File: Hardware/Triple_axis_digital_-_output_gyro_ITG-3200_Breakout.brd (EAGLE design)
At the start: 17.8 x 21.6 mm, 17 parts, among them U1 ITG-32001:1

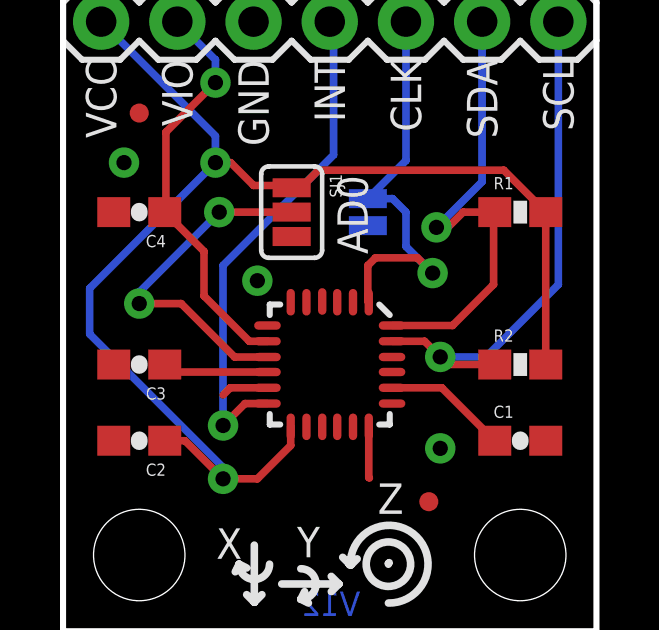
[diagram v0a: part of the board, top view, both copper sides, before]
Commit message: Changed a few trace routes
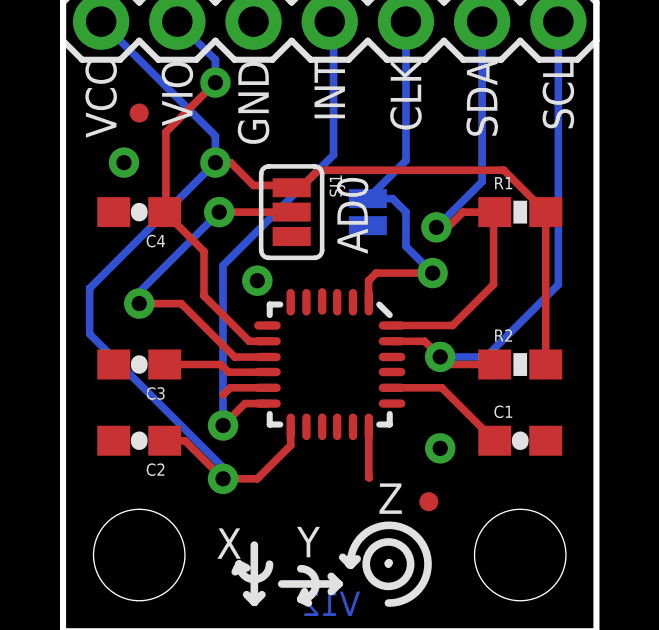
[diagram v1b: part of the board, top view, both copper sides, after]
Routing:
- net CLKIN: track 14.0 -> 13.2 mm
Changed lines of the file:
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@@
 <wire x1="33.02" y1="-3.683" x2="33.909" y2="-4.572" width="0.254" layer="16"/>
 <via x="33.909" y="-4.572" extent="1-16" drill="0.508"/>
-<wire x1="33.909" y1="-4.572" x2="33.401" y2="-4.064" width="0.254" layer="1"/>
-<wire x1="33.401" y1="-4.064" x2="32.004" y2="-4.064" width="0.254" layer="1"/>
-<wire x1="32.004" y1="-4.064" x2="31.75" y2="-4.318" width="0.254" layer="1"/>
-<wire x1="31.75" y1="-4.318" x2="31.75" y2="-5.513" width="0.254" layer="1"/>
-<wire x1="31.75" y1="-5.513" x2="31.7808" y2="-5.5438" width="0.254" layer="1"/>
+<wire x1="31.7808" y1="-5.5438" x2="31.7754" y2="-5.5384" width="0.254" layer="1"/>
+<wire x1="31.7754" y1="-5.5384" x2="31.7754" y2="-4.826" width="0.254" layer="1"/>
+<wire x1="31.7754" y1="-4.826" x2="32.0294" y2="-4.572" width="0.254" layer="1"/>
+<wire x1="32.0294" y1="-4.572" x2="33.909" y2="-4.572" width="0.254" layer="1"/>
 </signal>
 <signal name="INT">
@@
 <contactref element="C3" pad="1"/>
 <contactref element="U1" pad="10"/>
-<wire x1="28.4038" y1="-7.87" x2="25.23" y2="-7.87" width="0.254" layer="1"/>
-<wire x1="25.23" y1="-7.87" x2="24.98" y2="-7.62" width="0.254" layer="1"/>
+<wire x1="28.4038" y1="-7.87" x2="28.3998" y2="-7.874" width="0.254" layer="1"/>
+<wire x1="28.3998" y1="-7.874" x2="27.1018" y2="-7.874" width="0.254" layer="1"/>
+<wire x1="27.1018" y1="-7.874" x2="26.8478" y2="-7.62" width="0.254" layer="1"/>
+<wire x1="26.8478" y1="-7.62" x2="24.98" y2="-7.62" width="0.254" layer="1"/>
 </signal>
 <signal name="N$1">

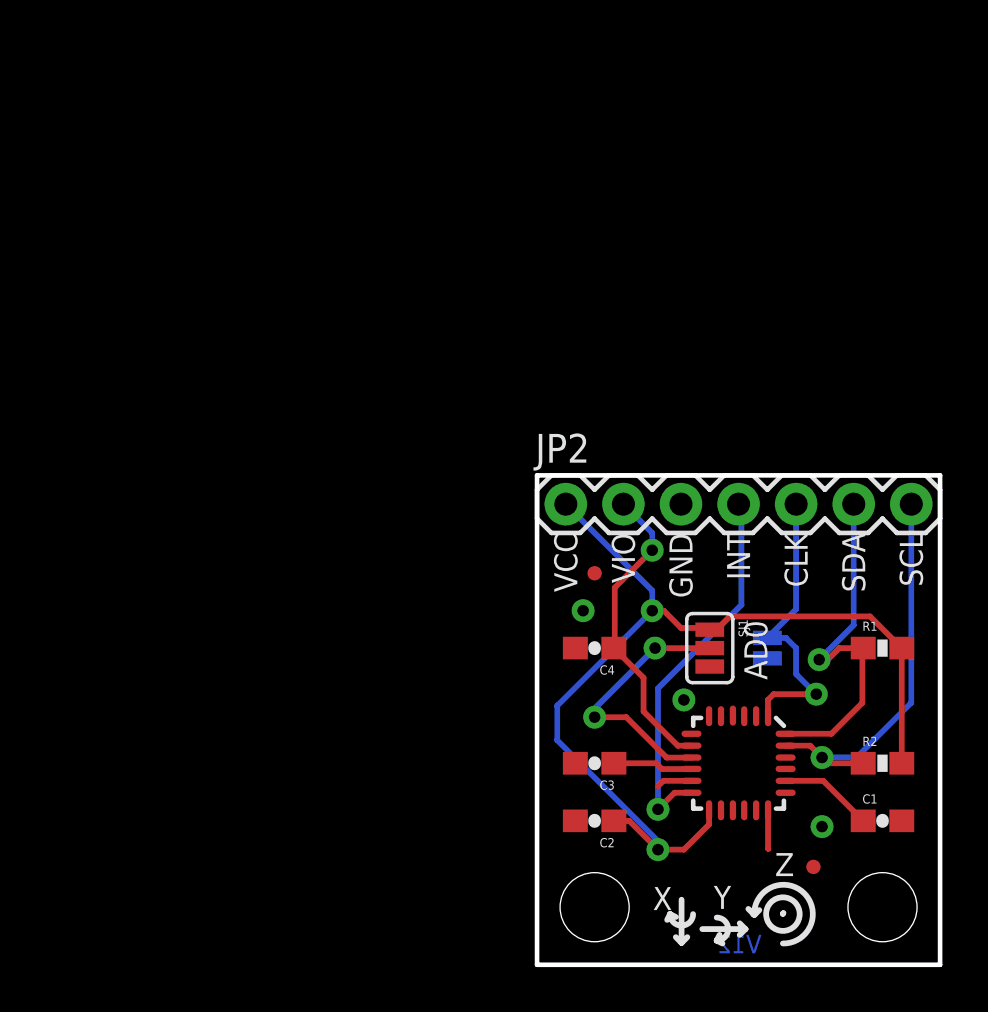
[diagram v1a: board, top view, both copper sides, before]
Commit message: re-routed traces to enter pads at a 90
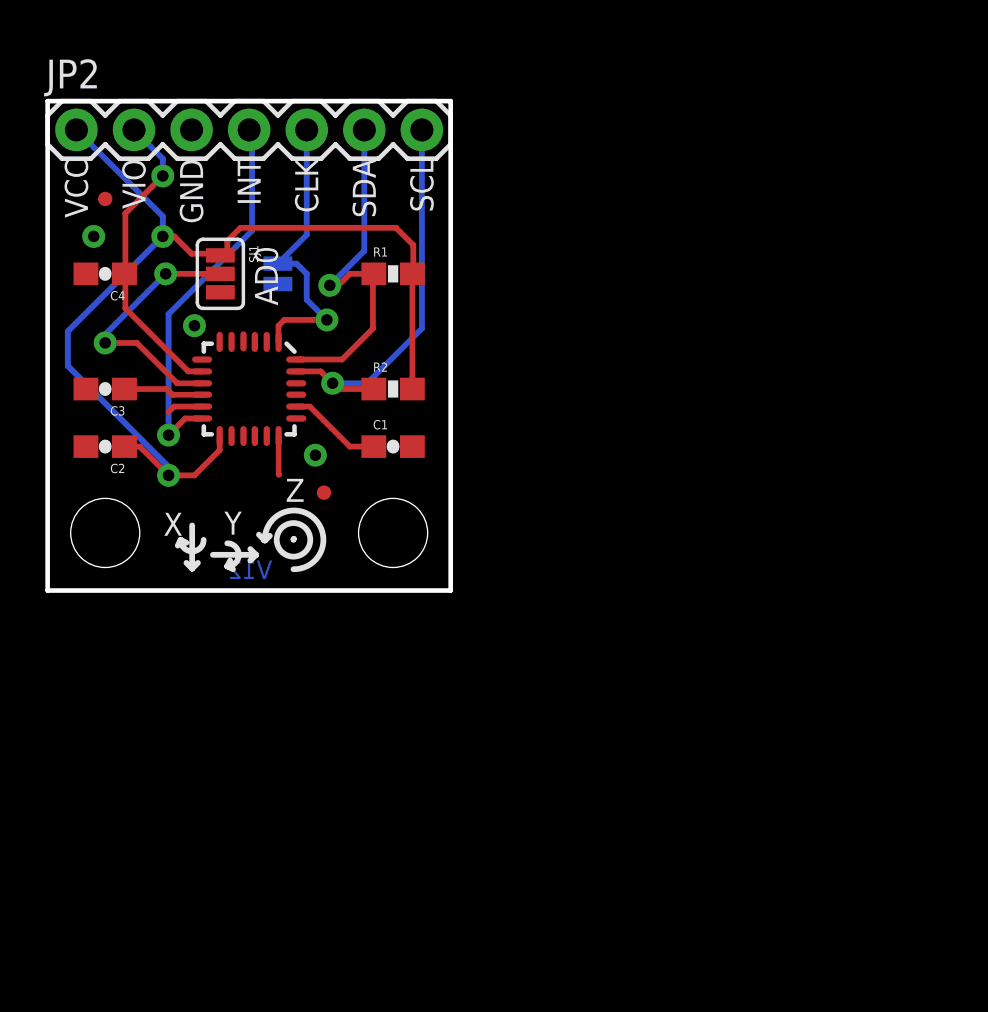
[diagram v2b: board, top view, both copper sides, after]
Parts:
- moved FRAME1 49.5 mm to (-27.9, -15.2)
- moved C3 27.2 mm to (2.54, 8.89)
- moved C4 27.2 mm to (2.54, 14.0)
- moved JP2 27.2 mm to (1.27, 20.3)
- moved JP6 27.2 mm to (10.2, 14.0)
- moved SJ1 27.2 mm to (7.62, 14.0)
- moved U$2 27.2 mm to (2.54, 2.54)
- moved U1 27.2 mm to (8.89, 8.89)
- moved C1 27.2 mm to (15.2, 6.35)
- moved C2 27.2 mm to (2.54, 6.35)
- moved FID1 27.2 mm to (2.54, 17.3)
- moved FID2 27.2 mm to (12.2, 4.32)
- moved LOGO1 27.2 mm to (9.09, 3.73)
- moved LOGO2 27.2 mm to (9.53, 8.13)
- moved R1 27.2 mm to (15.2, 14.0)
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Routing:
- net VCC: track 43.5 -> 45.2 mm

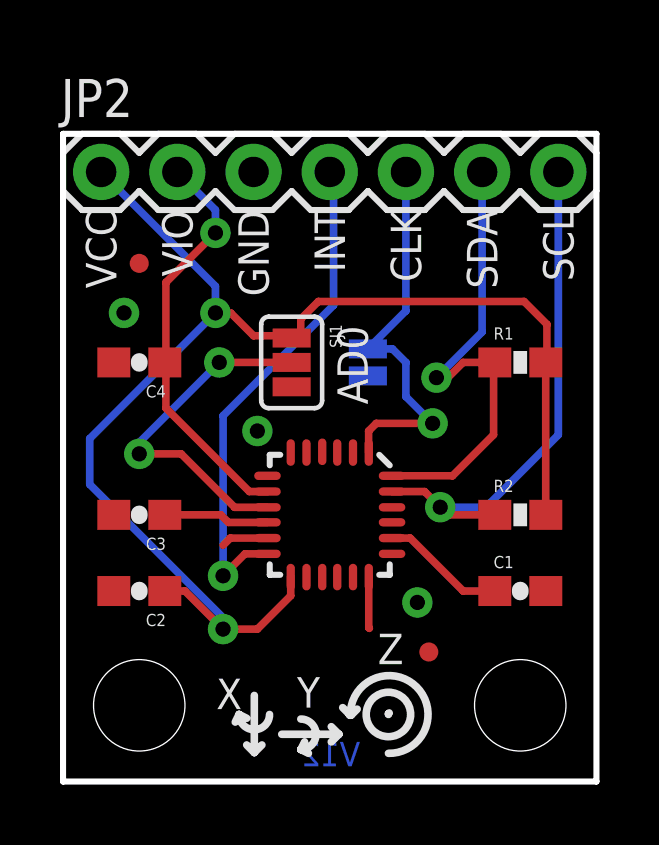
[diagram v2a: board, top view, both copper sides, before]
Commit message: Post Eng. Review fixes
-Moved axis symbols to be centered with the IC
-Added pull-up res. for ADO line/jumper
-Labeled bottom jumper
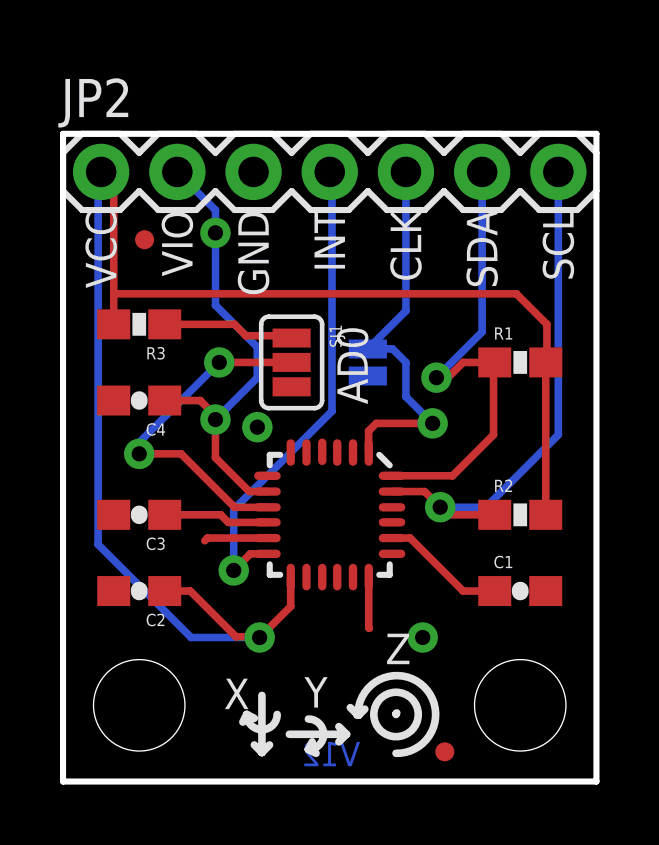
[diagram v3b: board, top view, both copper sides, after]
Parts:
- added R3: 10K, SparkFun-Resistors:0603-RES
- moved FID2 3.37 mm to (12.7, 0.99)
- moved C4 1.27 mm to (2.54, 12.7)
- moved FID1 0.81 mm to (2.72, 18.1)
- moved LOGO1 0.20 mm to (8.89, 3.73)
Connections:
- new net N$3: R3.1, SJ1.1
- net VCC: now also R3.2; no longer SJ1.1
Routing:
- net VCC: track 45.2 -> 51.9 mm, vias 2 -> 1
- net N$3: track 0.00 -> 4.42 mm
- net VLOGIC: track 13.7 -> 15.4 mm, vias 1 -> 2
- net INT: track 16.8 -> 16.0 mm
- net GND: track 3.30 -> 3.84 mm, vias 3 -> 2
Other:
- board text added: "CLKIN"
